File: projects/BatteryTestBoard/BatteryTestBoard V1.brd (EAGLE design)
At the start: 188.8 x 115.1 mm, 139 parts, among them M2 IPB120P04P4L03ATMA1, SW1 BTS50015-1TAD, U1 LTC4121-4.2, U2 AD8418, U3 AD8418, U4 LC05111C13MTTTG, U5 LTC4121, U6 AP9211SA-AG-HAC-7, U7 VNS3NV04DP-E

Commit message: included Ryan feedback
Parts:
- removed V17: LifePo cell 1, BrownSpaceEngineering:VIA-60MIL-SQ
- R19: device BrownSpaceEngineering:0805 -> BrownSpaceEngineering:1210
- R4, R5, R6, R7: device BrownSpaceEngineering:1210 -> BrownSpaceEngineering:0805
- V1, V37: value LION1 -> LION_OUTPUT
- V12: value Current sense -> LIONISNSREF
- V21, V26: value LF_B1 -> LIFEPO_OUT
- V34, V35: value LION_IN -> LION_CHARGER_IN
- V43: value Current sense -> LION_ISNS
- V58: value LifePo cell 1 -> LifePo Ref 1
- V59: value LifePo cell 2 -> LifePo Ref 2
- V75, V9: value LFPO_IN -> LFPO_CHARGER_IN
- moved R8 32.5 mm to (25.8, 27.7)
- moved R21 13.9 mm to (69.2, 61.7)
- moved C2 7.73 mm to (62.5, 67.2), turned to 0 degrees
- moved R20 7.01 mm to (54.7, 65.3)
- moved V16 5.59 mm to (131.7, 32.5)
- moved V34 5.21 mm to (38.7, 101.5)
- moved V35 5.21 mm to (33.1, 101.5)
- moved U4 4.71 mm to (62.4, 62.1)
- moved V20 1.78 mm to (179.2, 31.0)
- moved V62 0.13 mm to (93.9, 95.1)
- moved V65 0.13 mm to (93.9, 107.8)
- moved V69 0.13 mm to (93.9, 101.5)
- moved V54 0.13 mm to (87.5, 95.1)
- moved V61 0.13 mm to (87.5, 101.5)
- moved V68 0.13 mm to (87.5, 107.8)
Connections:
- removed net N$4: C1.2, C2.2, R24.P$2, R3.P$2, R8.P$1, U4.S1, U4.TST, U4.VSS, U6.S1, U6.VSS
- new net N$9: C1.2, C2.2, R24.P$2, R3.P$2, R8.P$1, U2.P$1, U4.P$3, U4.P$6, U6.S1
- net 3V3: now also R5.2, R7.2; no longer R5.P$2, R7.P$2
- net GND: now also R19.P$1, R4.1, R6.1, U4.P$1, U4.P$4, U6.VSS; no longer R19.1, R4.P$1, R6.P$1, U2.P$1, U4.S2
- net LFPOBAT: no longer V17.P$1
- net LFPOFREQ: now also R6.2, R7.1; no longer R6.P$2, R7.P$1
- net LFPOSNS+: now also R19.P$2; no longer R19.2
- net LIONFREQ: now also R4.2, R5.1; no longer R4.P$2, R5.P$1
- net N$14: now also U4.P$2; no longer U4.CS
- net N$8: now also U4.P$5; no longer U4.VCC
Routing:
- net N$9: track 0.00 -> 108.0 mm, vias 0 -> 4
- net N$4: track 87.5 -> 0.00 mm, vias 4 -> 0
- net 3V3: track 41.6 -> 3.22 mm, vias 7 -> 0
- net !LIONFAULT: track 45.9 -> 75.5 mm, vias 4 -> 0
- net N$3: track 24.2 -> 0.00 mm
- net !LIONCHRG: track 56.8 -> 77.5 mm, vias 3 -> 0
- net N$8: track 26.1 -> 12.4 mm
- net LIONBAT: track 170.8 -> 177.0 mm
- net LFPOBAT: track 141.1 -> 134.9 mm
- net N$7: track 24.4 -> 28.8 mm
- net LION_IN: track 44.8 -> 41.0 mm
- net N$14: track 8.66 -> 5.19 mm
- net LFPOSNS+: track 40.4 -> 37.7 mm, vias 2 -> 1
- net LFPORUN: track 49.5 -> 47.0 mm
- net LIONSNS+: track 43.7 -> 41.2 mm
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- added copper zone on layer 1, net 3V3
- added copper zone on layer 16, net GND
- added copper zone on layer 1, net N$3
- removed copper zone on layer 3, net 3V3
- removed copper zone on layer 2, net GND
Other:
- board size 188.8 x 115.1 mm -> 188.8 x 115.2 mm
- board text added: "Brown Space Eng. EQUiSat Aug. 17 Battery Test Board V1"
- board text added: "Li-ion charger in"
- board text added: "LifePo charger in"
- board text removed: "Brown Space Eng. Battery Test Board V1 July/August 2017"
- board text removed: "Li-ion in"
- board text removed: "LifePo in"
- board text removed: "reference voltage"

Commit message: Incorporating Ryan comments
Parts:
- added R26, R29, R30, R31: 0R, BrownSpaceEngineering:0805
- LIFEPO2: device BrownSpaceEngineering:EQUISAT-BATTERY-VB -> BrownSpaceEngineering:EQUISAT-BATTERY-VA
- moved R19 10.1 mm to (103.4, 65.0), turned to 90 degrees
- moved V21 10.0 mm to (173.1, 39.4)
- moved C2 9.94 mm to (54.7, 61.0), turned to 270 degrees
- moved V26 9.91 mm to (181.4, 39.4)
- moved R4 8.92 mm to (56.6, 95.1)
- moved R5 8.92 mm to (56.6, 99.6)
- moved V20 8.01 mm to (178.9, 23.0)
- moved V31 7.37 mm to (178.9, 30.4)
- moved R48 6.66 mm to (92.8, 47.5)
- moved V59 6.66 mm to (86.2, 48.4)
- moved M1 6.63 mm to (165.7, 42.2)
- moved C1 5.33 mm to (55.2, 46.2), turned to 90 degrees
- moved R12 5.21 mm to (90.3, 39.5)
- moved U3 5.21 mm to (95.0, 39.9)
- moved V11 5.21 mm to (90.3, 27.3)
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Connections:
- new net N$10: R30.1, R31.1, U4.P$4
- new net N$4: R26.1, R29.2, U6.VSS
- net 3V3: no longer R5.2, R7.2
- net GND: now also R26.2, R30.2; no longer U4.P$4, U6.VSS
- net LFPOINTVCC: now also R7.2
- net LIONINTVCC: now also R5.2
- net N$9: now also R29.1, R31.2
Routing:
- net GND: track 144.9 -> 105.2 mm, vias 39 -> 40
- net N$9: track 108.0 -> 146.2 mm, vias 4 -> 2
- net LIONBAT: track 177.0 -> 155.9 mm, vias 2 -> 3
- net LFPOINTVCC: track 36.6 -> 56.2 mm, vias 0 -> 2
- net LIONINTVCC: track 31.2 -> 46.0 mm, vias 1 -> 3
- net N$4: track 0.00 -> 12.5 mm, vias 0 -> 2
- net N$7: track 28.8 -> 18.6 mm
- net LIONFREQ: track 59.8 -> 49.6 mm, vias 4 -> 3
- net N$10: track 0.00 -> 7.88 mm
- net LFPOCHGSNS: track 50.2 -> 57.4 mm
- net LFPOSNS+: track 37.7 -> 30.6 mm, vias 1 -> 2
- net LIFE2: track 72.4 -> 79.4 mm
- net FUSE_OUT: track 15.2 -> 21.0 mm
- net LF_B1_OUTEN: track 31.7 -> 36.8 mm, vias 2 -> 1
- net LIONMPPT: track 35.9 -> 40.7 mm
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- added copper zone on layer 1, net LIONBAT
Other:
- board text added: "GND (750KHz)"
- board text added: "INTVCC (1.5MHz)"
- board text removed: "3.3V"

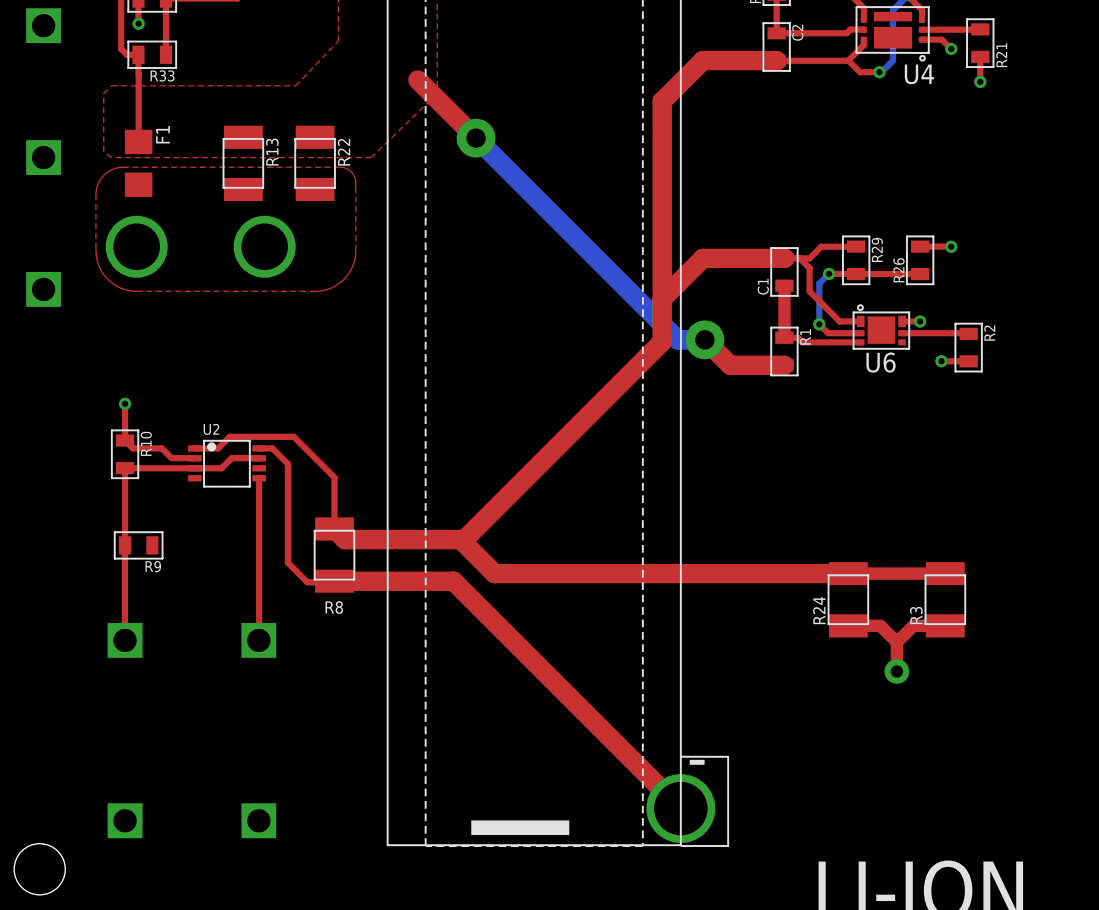
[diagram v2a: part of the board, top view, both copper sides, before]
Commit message: Better current sense routing
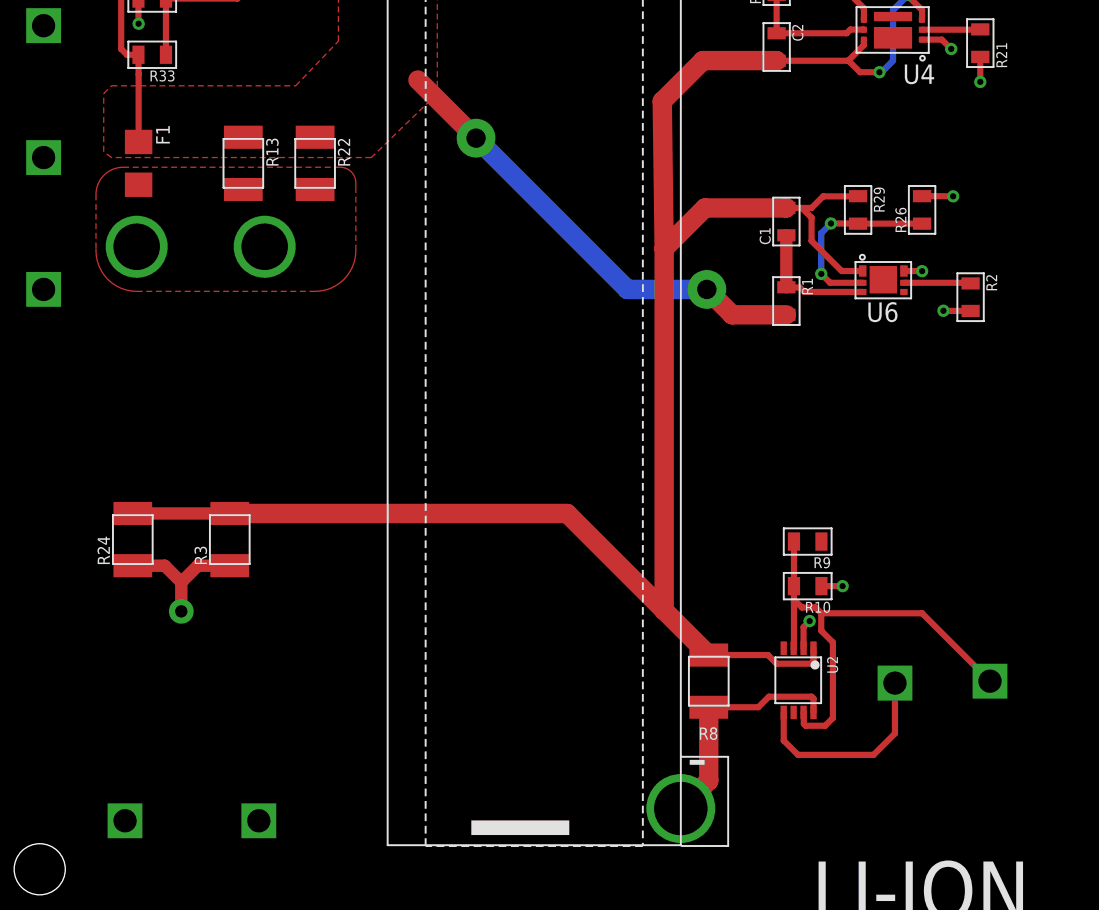
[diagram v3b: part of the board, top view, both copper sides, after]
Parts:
- moved V12 56.7 mm to (68.7, 19.4)
- moved R24 47.0 mm to (12.6, 28.7)
- moved R3 47.0 mm to (18.9, 28.7)
- moved R10 45.5 mm to (56.8, 25.7), turned to 180 degrees
- moved R9 43.8 mm to (56.8, 28.6)
- moved U2 42.6 mm to (57.1, 21.6), turned to 180 degrees
- moved V43 41.7 mm to (62.5, 19.3)
- moved R8 25.9 mm to (50.3, 19.4)
- moved C1 3.30 mm to (55.4, 49.5)
- moved R1 3.30 mm to (55.4, 44.3)
- moved R2 3.30 mm to (67.4, 44.6)
- moved R26 3.30 mm to (64.3, 50.3)
- moved R29 3.30 mm to (60.1, 50.3)
- moved U6 3.30 mm to (61.7, 45.7)
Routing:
- net LIONSNS+: track 41.2 -> 15.5 mm
- net N$11: track 20.4 -> 32.1 mm
- net N$9: track 146.2 -> 139.7 mm
- net GND: track 105.2 -> 101.0 mm, vias 40 -> 41
- net L1_SNS: track 10.6 -> 13.4 mm
- net LIONBAT: track 155.9 -> 154.7 mm

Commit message: Final changes to board
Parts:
- moved R21 3.18 mm to (69.0, 64.3)
- moved R2 2.16 mm to (69.3, 43.6)
- moved C23 1.91 mm to (178.3, 44.8)
- moved R26 1.40 mm to (65.7, 50.3)
- moved R29 1.40 mm to (61.5, 50.3)
- moved R1 1.02 mm to (55.4, 43.3)
- moved U6 1.02 mm to (61.7, 44.7)
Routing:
- net GND: track 101.0 -> 137.8 mm, vias 41 -> 42
- net LFPOBAT: track 134.9 -> 114.9 mm, vias 2 -> 1
- net LF_B1_OSNS: track 38.5 -> 42.8 mm
- net LF2_REF: track 6.61 -> 10.4 mm
- net LF1_REF: track 6.61 -> 10.4 mm
- net LIONBAT: track 154.7 -> 157.4 mm
- net N$14: track 3.83 -> 5.99 mm
- net N$1: track 4.38 -> 6.29 mm
- net N$9: track 139.7 -> 141.4 mm
- net N$4: track 12.5 -> 14.1 mm
- net N$5: track 8.57 -> 9.59 mm
- net N$11: track 32.1 -> 32.7 mm
- net LIFE2: track 79.4 -> 79.5 mm, vias 0 -> 2

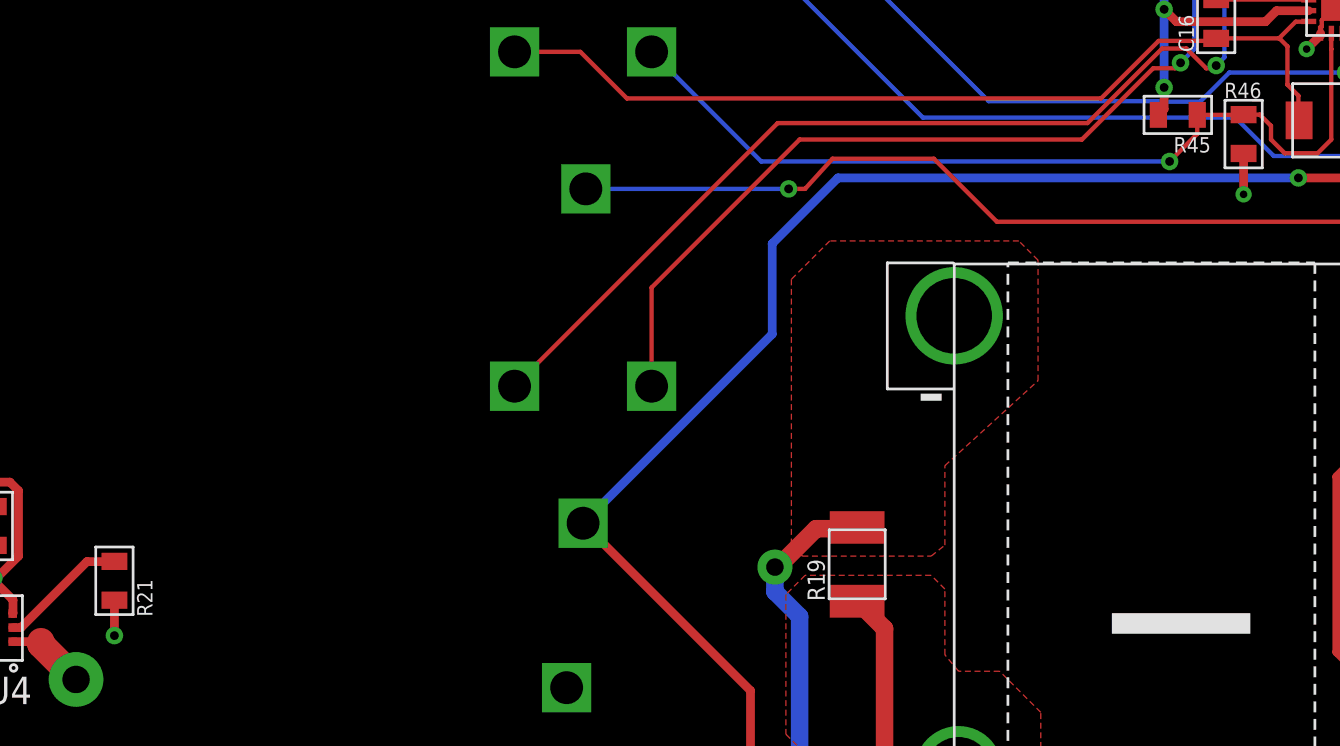
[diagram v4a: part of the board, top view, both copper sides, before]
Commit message: Silkscreen text vectorized
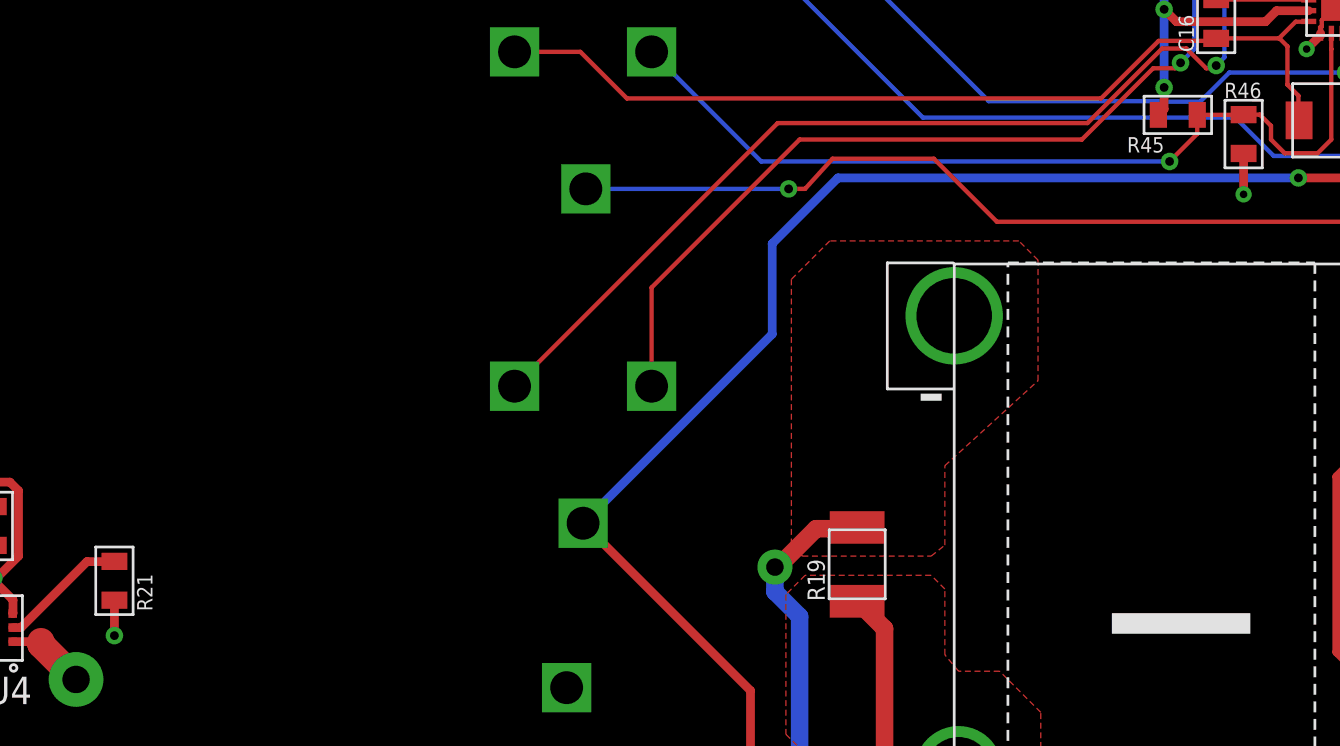
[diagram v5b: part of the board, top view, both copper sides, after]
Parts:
- V16: value LifePo cell 2 -> Cell 2
